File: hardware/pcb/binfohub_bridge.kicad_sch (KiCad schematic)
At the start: 48 parts, among them J1 12V IN, J2 BUS A B, J3 IH 12V GND A B, J4 LED OUT, Q1 AO3401A, U1 ESP32-DevKitC-32 (38-pin), U2 AP63205WU-7, U3 SP3485EN, U4 SP3485EN

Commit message: Hardware rev 1.1: bare WROOM-32E, 3.3 V rail, fan header, programming header
Same outline, holes, terminal and LED positions as rev 1.0, so it fits the
existing enclosure. Driven by the 2026-10-01 thermal failure: ESP32-WROOM-32E
soldered at the right edge (antenna outward; -32UE fits the same pads for a
U.FL remote antenna), AP63203 3.3 V buck replacing the 5 V rail and the
DevKit's linear regulator, J5 12 V PWM fan output (IO32, AO3400A, F3, SS14),
EN/IO0 support with RESET/BOOT and a J6 programming header, R10/R11 bias.

ERC 0, DRC 0 errors / 0 unconnected (7 cosmetic warnings), 100 % routed
(755 tracks / 104 vias), ground pour plotted. Rev 1.0's shipped gerbers had
no pour (zone outlines were never refilled at plot time); export.sh now
refills and counts regions. Router gains a --trim-only mode and a junction-
aware dangling-end trim. packages/fan.yaml added (commented include; RAM
83.0 %, see its header). Rev 1.0 files tagged pcb-rev1.0.

Co-Authored-By: Claude Fable 5.1 <noreply@anthropic.com>
Claude-Session: https://claude.ai/code/session_01ESVh7DpLzA3jfcrFtGgM8a
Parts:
- added C11: 1uF 50V, Capacitor_SMD:C_0603_1608Metric, symbol Device:C
- added D10: SS14, Diode_SMD:D_SMA, symbol Device:D_Schottky
- added F3: 0.5A polyfuse 1812, Fuse:Fuse_1812_4532Metric, symbol Device:Polyfuse
- added J5: FAN 12V, TerminalBlock_Phoenix:TerminalBlock_Phoenix_MPT-0,5-2-2.54_1x02_P2.54mm_Horizontal, symbol Connector_Generic:Conn_01x02
- added J6: PROG, Connector_PinHeader_2.54mm:PinHeader_1x06_P2.54mm_Vertical, symbol Connector_Generic:Conn_01x06
- added Q2: AO3400A, Package_TO_SOT_SMD:SOT-23, symbol Transistor_FET:AO3400A
- added R10, R11: 4k7, Resistor_SMD:R_0603_1608Metric, symbol Device:R
- added R12: 100R, Resistor_SMD:R_0603_1608Metric, symbol Device:R
- added R13, R14, R15: 10k, Resistor_SMD:R_0603_1608Metric, symbol Device:R
- added SW1, SW2: TS-1187A, binfohub:SW_TS-1187A, symbol Switch:SW_Push
- C7: value 22uF 25V -> 10uF 25V; LCSC C45783 -> C15850
- R5: value 330R -> 100R; LCSC C23138 -> C22775
- U1: value ESP32-DevKitC-32 (38-pin) -> ESP32-WROOM-32E; footprint binfohub:ESP32-DevKitC-38 -> binfohub:ESP32-WROOM-32E_edge; symbol binfohub:ESP32-DevKitC-38 -> RF_Module:ESP32-WROOM-32E; LCSC (none) -> C2973652
- U2: value AP63205WU-7 -> AP63203WU-7; symbol Regulator_Switching:AP63205WU -> Regulator_Switching:AP63203WU; LCSC C2071056 -> C780769
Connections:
- net +12V: now also F3.1
- net +3V3: now also C7.1, C8.1, F1.2, R5.1, U1.2 (VDD), J6.1 (Pin_1), R10.1, R14.1, R15.1; no longer U1.1 (3V3)
- net A_DE: now also U1.26 (IO4); no longer U1.32 (IO4)
- net A_DI: now also U1.28 (IO17); no longer U1.30 (IO17)
- net A_RO: now also U1.27 (IO16); no longer U1.31 (IO16)
- net B_DE: now also U1.33 (IO21); no longer U1.25 (IO21)
- net B_DI: now also U1.36 (IO22); no longer U1.22 (IO22)
- net B_RO: now also U1.37 (IO23); no longer U1.21 (IO23)
- net GND: now also U1.[1,15,38,39] (GND), C11.2, J6.2 (Pin_2), Q2.2 (S), R11.2, R13.2, SW1.2, SW2.2; no longer U1.14 (GND), U1.20 (GND), U1.26 (GND)
- net IH_A: now also R10.2
- net IH_B: now also R11.1
- net LED_BUS: now also U1.11 (IO26); no longer U1.10 (IO26)
- net LED_FAULT: now also U1.12 (IO27); no longer U1.11 (IO27)
- net LED_WIFI: now also U1.10 (IO25); no longer U1.9 (IO25)
- net ESP_EN: now reaches U1.3 (EN)
- net ESP_EN: now also C11.1, J6.5 (Pin_5), R14.2, SW1.1
- net ESP_RXD0: now reaches U1.34 (RXD0/IO3)
- net ESP_RXD0: now also J6.4 (Pin_4)
- net ESP_TXD0: now reaches U1.35 (TXD0/IO1)
- net ESP_TXD0: now also J6.3 (Pin_3)
- net FAN_PWM: now reaches U1.8 (IO32)
- net FAN_PWM: now also R12.1
- removed net +5V: C7.1, C8.1, F1.2, R5.1, U1.19 (5V)
- net 5V_BUCK renamed 3V3_BUCK
- new net ESP_IO0: J6.6 (Pin_6), R15.2, SW2.1, U1.25 (IO0)
- new net FAN_12V: D10.1 (K), F3.2, J5.2 (Pin_2)
- new net FAN_G: Q2.1 (G), R12.2, R13.1
- new net FAN_SW: D10.2 (A), J5.1 (Pin_1), Q2.3 (D)
- no-connect marks 24 -> 20
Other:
- note added: "3.3 V RAIL: AP63203WU-7 sync buck, 3.8-32 V in, fixed 3.3 V 2 A (circuit from b-hydro carrier v2.1)."
- note added: "B-INFOHUB BRIDGE v1.1 -- Briggs & Stratton GC-1032 RS-485 bridge with InfoHub passthrough"
- note added: "EN/BOOT: 10k pull-ups, 1 uF on EN. SW1 RESET, SW2 BOOT (diagonal pads only -- see circuit.py)."
- note added: "ESP32-WROOM-32E soldered (rev 1.1; was a socketed DevKitC). Same pads take the -32UE"
- note added: "J4 EXT LED: the same anode nodes, for panel LEDs in parallel. FAN (rev 1.1): 12 V via F3,"
- note added: "J6 PROG: 3V3 GND TX RX EN IO0 -- first flash with any 3.3 V USB-serial adapter, OTA after that."
- note added: "Q2 low-side PWM from IO32, D10 flyback, R13 holds the fan OFF while the ESP is in reset."
- note added: "Rev 1.1: one rail. The 5 V rail only fed the DevKit's linear 3.3 V regulator, which is gone."
- note added: "at slave 10 so the InfoHub keeps working. R10/R11 bias the idle pair (rev 1.1)."
- note added: "for a U.FL remote antenna. No strapping pin carries a function; IO0 is BOOT only."
- note added: "the bridge is actually transmitting, not merely powered. All on 3.3 V, 100R blue/green."
- note removed: "5 V RAIL: AP63205WU-7 sync buck, 3.8-32 V in, fixed 5 V 2 A (from b-hydro carrier v2.1)"
- note removed: "B-INFOHUB BRIDGE v1.0 -- Briggs & Stratton GC-1032 RS-485 bridge with InfoHub passthrough"
- note removed: "ESP32-DevKitC-38, socketed. Use the -32U variant for an external antenna."
- note removed: "EXTERNAL LED HEADER: the on-board LEDs are invisible inside a sealed box."
- note removed: "J4 carries the same anode nodes so panel LEDs can sit in parallel."
- note removed: "No strapping pin (0/2/12/15) is used, so nothing here can stop it booting."
- note removed: "at slave 10 so the InfoHub keeps working (ESPHome modbus role: server + modbus_server)."
- note removed: "the bridge is actually transmitting, not merely powered."
- title: B-Infohub Bridge v1.0 -> B-Infohub Bridge v1.1
- moved on the sheet: C7, C8, H1, H2, H3, H4, H5, H6

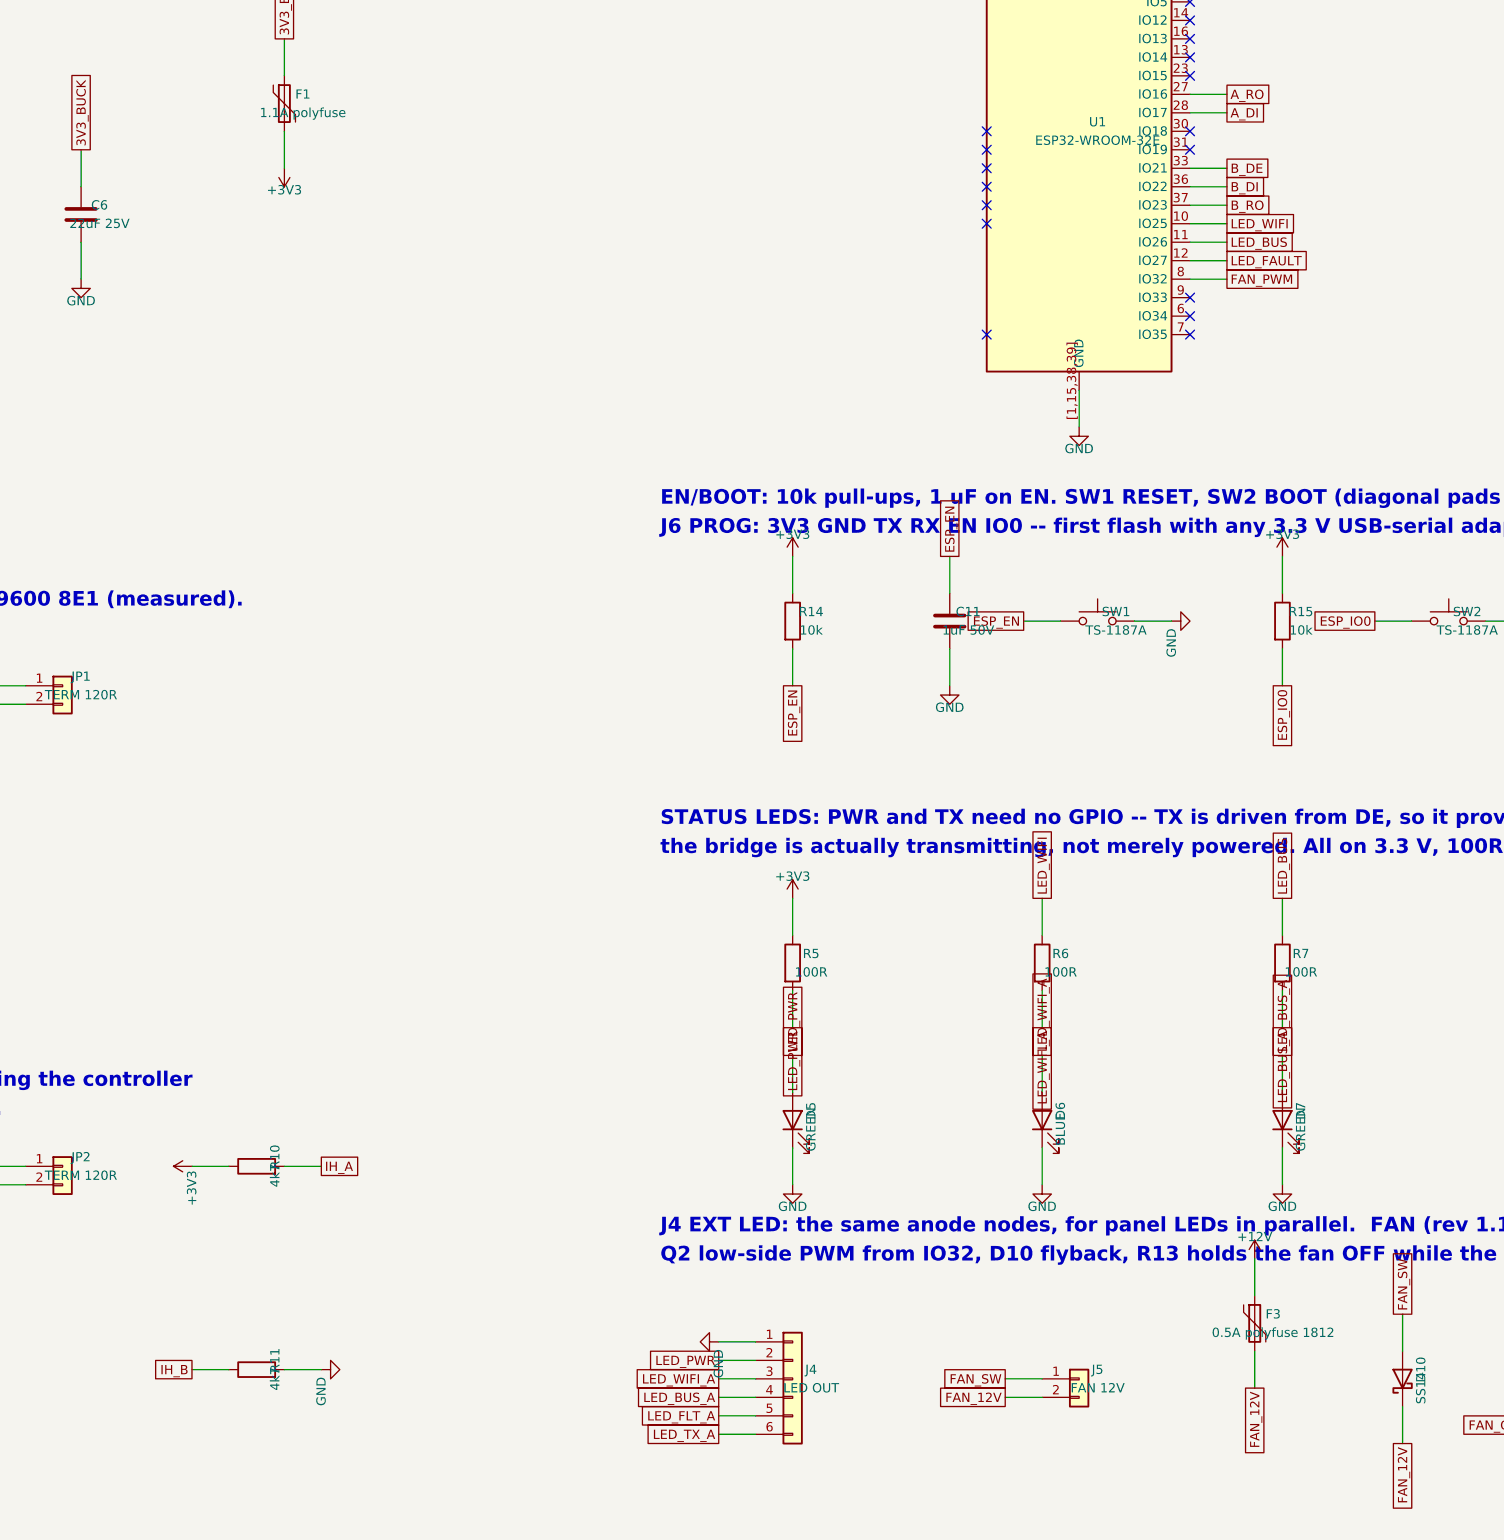
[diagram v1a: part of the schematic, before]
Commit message: PCB rev 1.1: EE review fixes
-H4 (105 C) module C3013935; DE pull-downs R16/R17 so neither transceiver can
drive the bus while the ESP is in reset or being flashed; 680R fail-safe bias
(covers a terminated far end); F3 1.1 A / 33 V (a 0.5 A PPTC derates below
any real fan at box temperature); 100 nF at the VDD pad; BOM grouped by part
so no LCSC number spans two lines; header rotation keys fixed; JLC gerber set
trimmed to fab layers. ERC 0, DRC 0 errors / 0 unconnected, 738 tracks / 109
vias, pour plotted.

Co-Authored-By: Claude Fable 5.1 <noreply@anthropic.com>
Claude-Session: https://claude.ai/code/session_01ESVh7DpLzA3jfcrFtGgM8a
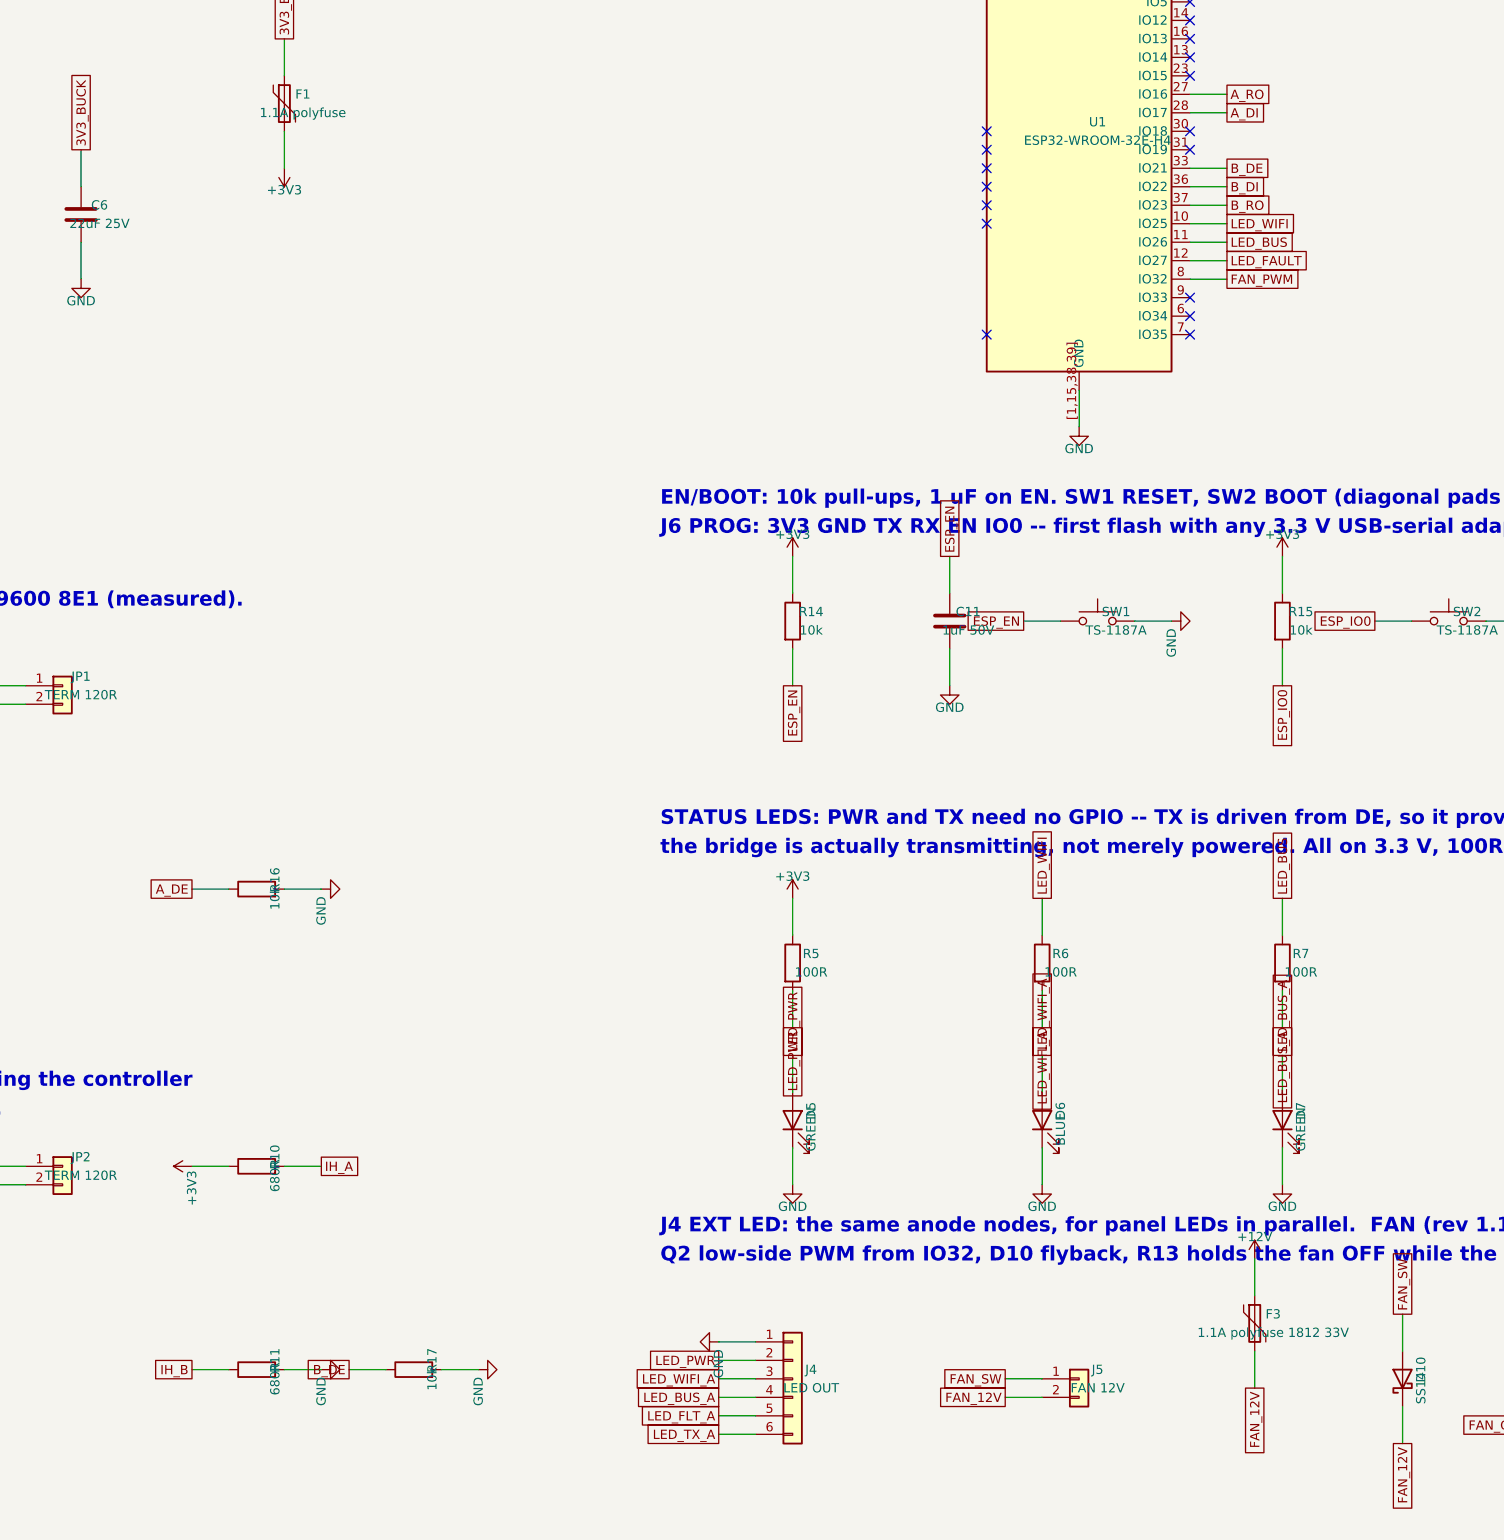
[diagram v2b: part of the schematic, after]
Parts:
- added R16, R17: 10k, Resistor_SMD:R_0603_1608Metric, symbol Device:R
- F3: value 0.5A polyfuse 1812 -> 1.1A polyfuse 1812 33V; LCSC C462518 -> C142747
- R10, R11: value 4k7 -> 680R; LCSC C23162 -> C23228
- U1: value ESP32-WROOM-32E -> ESP32-WROOM-32E-H4; LCSC C2973652 -> C3013935
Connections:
- net A_DE: now also R16.1
- net B_DE: now also R17.1
- net GND: now also R16.2, R17.2
